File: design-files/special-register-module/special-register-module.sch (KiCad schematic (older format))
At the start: 64 parts, among them U402 74HCT377, U403 74HCT161, U404 74HCT161, U405 74HCT245, U406 74HCT245, U407 74HCT08, U408 74HCT273, U409 74HCT245

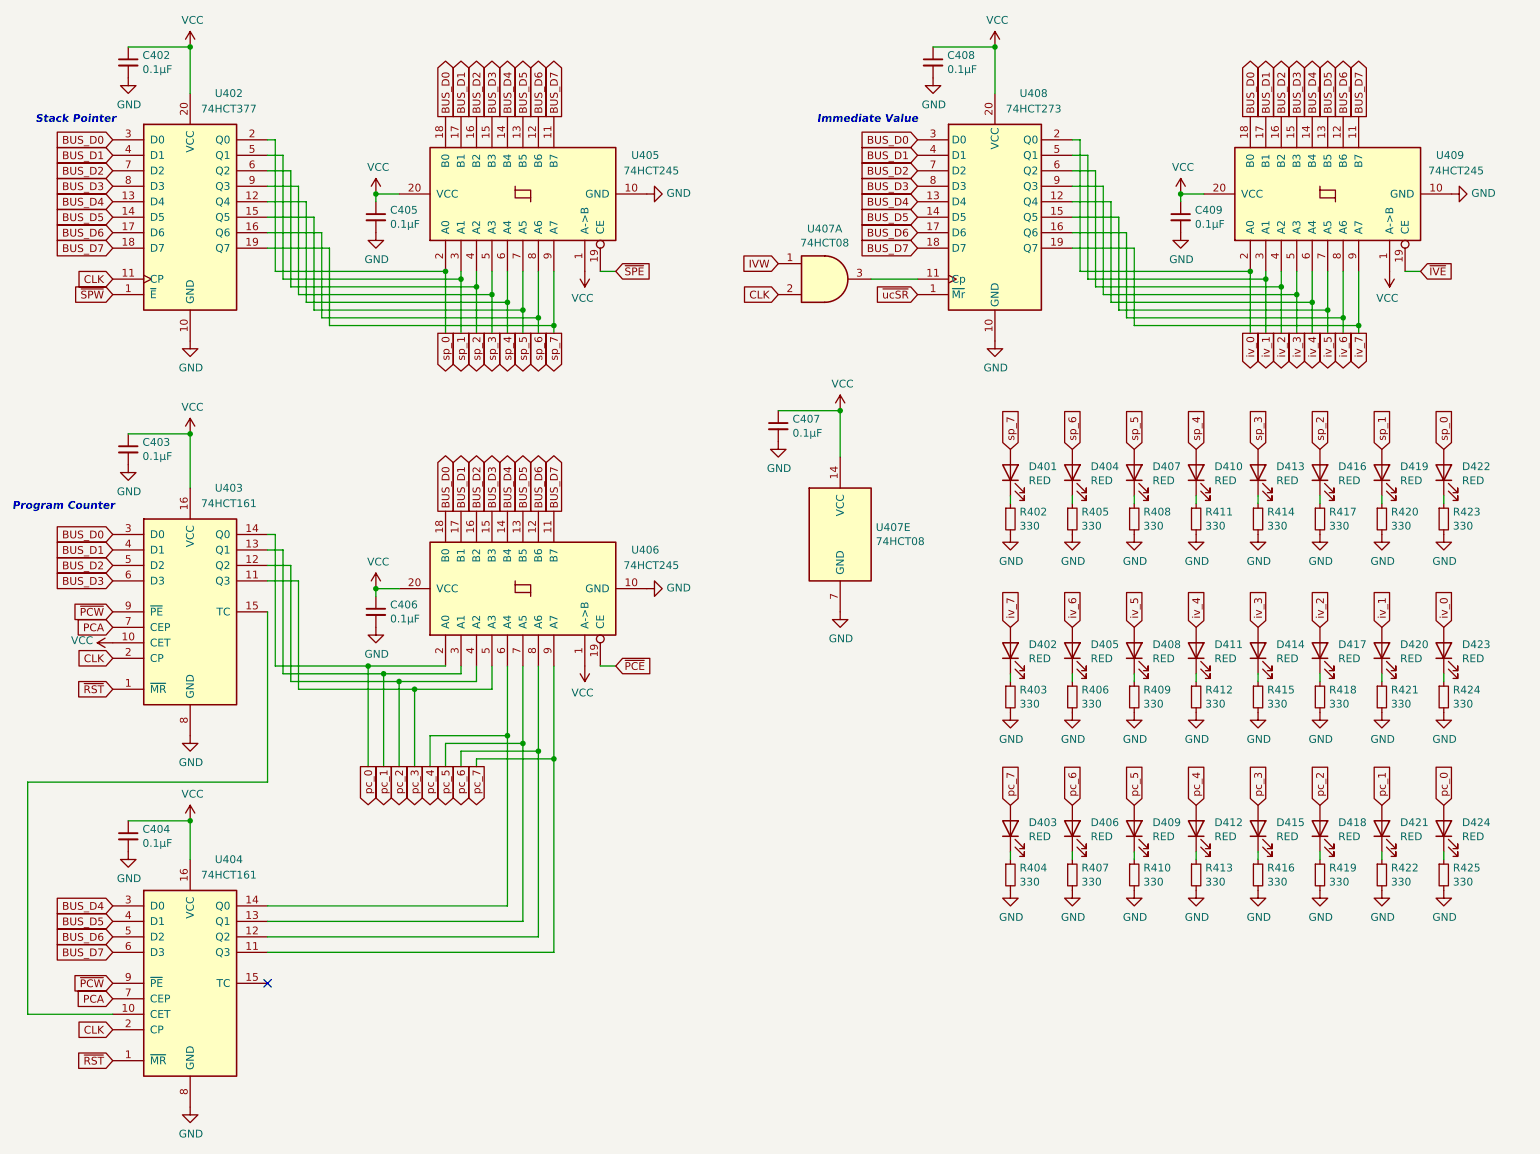
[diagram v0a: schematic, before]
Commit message: Rework to use DIP resistor packs for the LEDs.
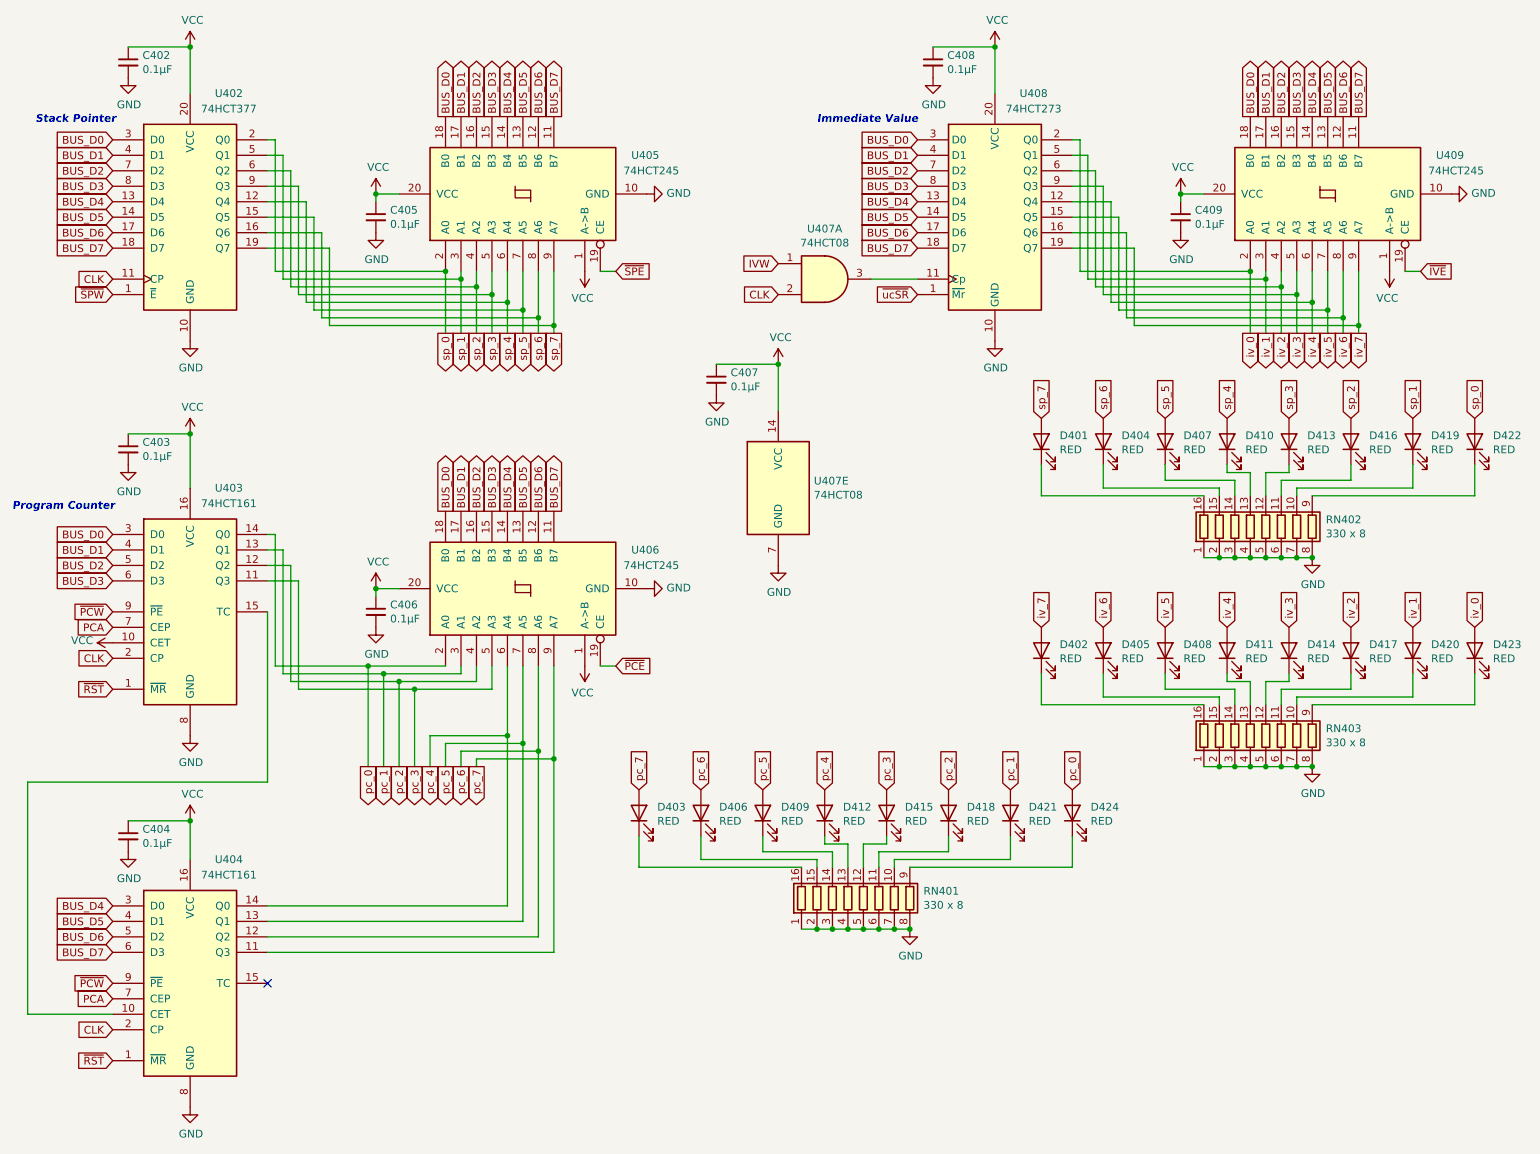
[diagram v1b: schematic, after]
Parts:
- removed R402, R403, R404, R405, R406, R407, R408, R409, R410, R411, R412, R413, R414, R415, R416, R417, R418, R419, R420, R421, R422, R423, R424, R425: 330, Resistor_THT:R_Axial_DIN0204_L3.6mm_D1.6mm_P5.08mm_Horizontal, symbol Device:R_Small
- added RN401, RN402, RN403: 330 x 8, Package_DIP:DIP-16_W7.62mm_Socket, symbol Device:R_Pack08
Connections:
- net GND: now also RN401.1 (R1.1), RN401.2 (R2.1), RN401.3 (R3.1), RN401.4 (R4.1), RN401.5 (R5.1), RN401.6 (R6.1), RN401.7 (R7.1), RN401.8 (R8.1), RN402.1 (R1.1), RN402.2 (R2.1), RN402.3 (R3.1), RN402.4 (R4.1), RN402.5 (R5.1), RN402.6 (R6.1), RN402.7 (R7.1), RN402.8 (R8.1), RN403.1 (R1.1), RN403.2 (R2.1), RN403.3 (R3.1), RN403.4 (R4.1), RN403.5 (R5.1), RN403.6 (R6.1), RN403.7 (R7.1), RN403.8 (R8.1)
- net at D401.1 (K): now also RN402.16 (R1.2)
- net at D404.1 (K): now also RN402.15 (R2.2)
- net at D407.1 (K): now also RN402.14 (R3.2)
- net at D410.1 (K): now also RN402.13 (R4.2)
- net at D413.1 (K): now also RN402.12 (R5.2)
- net at D416.1 (K): now also RN402.11 (R6.2)
- net at D419.1 (K): now also RN402.10 (R7.2)
- net at D422.1 (K): now also RN402.9 (R8.2)
- net at D402.1 (K): now also RN403.16 (R1.2)
- net at D405.1 (K): now also RN403.15 (R2.2)
- net at D408.1 (K): now also RN403.14 (R3.2)
- net at D411.1 (K): now also RN403.13 (R4.2)
- net at D414.1 (K): now also RN403.12 (R5.2)
- net at D417.1 (K): now also RN403.11 (R6.2)
- net at D420.1 (K): now also RN403.10 (R7.2)
- net at D423.1 (K): now also RN403.9 (R8.2)
- net at D403.1 (K): now also RN401.16 (R1.2)
- net at D406.1 (K): now also RN401.15 (R2.2)
- net at D409.1 (K): now also RN401.14 (R3.2)
- net at D412.1 (K): now also RN401.13 (R4.2)
- net at D415.1 (K): now also RN401.12 (R5.2)
- net at D418.1 (K): now also RN401.11 (R6.2)
- net at D421.1 (K): now also RN401.10 (R7.2)
- net at D424.1 (K): now also RN401.9 (R8.2)
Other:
- moved on the sheet: C407, D401, D402, D403, D404, D405, D406, D407, D408, D409, D410, D411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

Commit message: Make the IV register a '377; there isn't really any reason to make it reset to 0 at the beginning of each instruction.
While here, fix the CC selector; Enable is active-low.
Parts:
- removed C407: 0.1µF, Capacitor_THT:C_Radial_D6.3mm_H5.0mm_P2.50mm, symbol Device:C_Small
- removed U407: 74HCT08, Package_DIP:DIP-14_W7.62mm_Socket, symbol 74xx:74LS08
- removed U408: 74HCT273, Package_DIP:DIP-20_W7.62mm_Socket, symbol 74xx:74LS273
- added U407: 74HCT377, symbol 74xx:74LS377
- renumbered U409 to U408
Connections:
- net BUS_D0: now also U407.3 (D0)
- net BUS_D1: now also U407.4 (D1)
- net BUS_D2: now also U407.7 (D2)
- net BUS_D3: now also U407.8 (D3)
- net BUS_D4: now also U407.13 (D4)
- net BUS_D5: now also U407.14 (D5)
- net BUS_D6: now also U407.17 (D6)
- net BUS_D7: now also U407.18 (D7)
- net CLK: now also U407.11 (CP)
- net GND: now also U407.10 (GND)
- net VCC: now also U407.20 (VCC)
- net iv_0: now also U407.2 (Q0)
- net iv_1: now also U407.5 (Q1)
- net iv_2: now also U407.6 (Q2)
- net iv_3: now also U407.9 (Q3)
- net iv_4: now also U407.12 (Q4)
- net iv_5: now also U407.15 (Q5)
- net iv_6: now also U407.16 (Q6)
- net iv_7: now also U407.19 (Q7)
- new net ~IVW: U407.1 (~E)
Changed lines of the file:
@@
 BUS_D7
 $Comp
-L 74xx:74LS245 U409
+L 74xx:74LS245 U408
 U 1 1 61BE426D
 P 9200 1700
-F 0 "U409" V 9450 1000 50  0000 R CNN
+F 0 "U408" V 9450 1000 50  0000 R CNN
 F 1 "74HCT245" V 9350 1050 50  0000 R CNN
 F 2 "Package_DIP:DIP-20_W7.62mm_Socket" H 9200 1700 50  0001 C CNN
@@
 Text GLabel 6550 2050 0    50   Input ~ 0
 BUS_D7
-Text GLabel 5650 2350 0    50   Input ~ 0
+Text GLabel 6550 2250 0    50   Input ~ 0
 CLK
-Text GLabel 5650 2150 0    50   Input ~ 0
-IVW
+Text GLabel 6550 2350 0    50   Input ~ 0
+~IVW
 Text GLabel 9800 2200 2    50   Input ~ 0
 ~IVE
@@
 Text GLabel 9400 1200 1    50   Output ~ 0
 BUS_D7
-$Comp
-L 74xx:74LS273 U408
-U 1 1 61BE6AF1
-P 7050 1850
-F 0 "U408" H 7300 2650 50  0000 C CNN
-F 1 "74HCT273" H 7300 2550 50  0000 C CNN
-F 2 "Package_DIP:DIP-20_W7.62mm_Socket" H 7050 1850 50  0001 C CNN
-F 3 "http://www.ti.com/lit/gpn/sn74LS273" H 7050 1850 50  0001 C CNN
-	1    7050 1850
-	1    0    0    -1
-$EndComp
-$Comp
-L 74xx:74LS08 U407
-U 1 1 61BE8065
-P 5950 2250
-F 0 "U407" H 5950 2575 50  0000 C CNN
-F 1 "74HCT08" H 5950 2484 50  0000 C CNN
-F 2 "Package_DIP:DIP-14_W7.62mm_Socket" H 5950 2250 50  0001 C CNN
-F 3 "http://www.ti.com/lit/gpn/sn74LS08" H 5950 2250 50  0001 C CNN
-	1    5950 2250
-	1    0    0    -1
-$EndComp
-Wire Wire Line
-	6250 2250 6550 2250
-Text GLabel 6550 2350 0    50   Input ~ 0
+Text GLabel 1250 2850 0    50   Input ~ 0
 ~ucSR
 Text Notes 850  1250 0    50   Italic 10
@@
 pc_7
 $Comp
-L 74xx:74LS08 U407
-U 5 1 61D03C75
-P 5650 3600
-F 0 "U407" H 5880 3646 50  0000 L CNN
-F 1 "74HCT08" H 5880 3555 50  0000 L CNN
-F 2 "Package_DIP:DIP-14_W7.62mm_Socket" H 5650 3600 50  0001 C CNN
-F 3 "http://www.ti.com/lit/gpn/sn74LS08" H 5650 3600 50  0001 C CNN
-	5    5650 3600
-	1    0    0    -1
-$EndComp
-$Comp
-L power:GND #PWR0136
-U 1 1 61D077EE
-P 5650 4100
-F 0 "#PWR0136" H 5650 3850 50  0001 C CNN
-F 1 "GND" H 5655 3927 50  0000 C CNN
-F 2 "" H 5650 4100 50  0001 C CNN
-F 3 "" H 5650 4100 50  0001 C CNN
-	1    5650 4100
-	1    0    0    -1
-$EndComp
-$Comp
 L Device:C_Small C402
 U 1 1 61D13B27
@@
 Connection ~ 7050 750
 $Comp
-L Device:C_Small C407
-U 1 1 61D67E66
-P 5250 2900
-F 0 "C407" H 5342 2946 50  0000 L CNN
-F 1 "0.1µF" H 5342 2855 50  0000 L CNN
-F 2 "Capacitor_THT:C_Radial_D6.3mm_H5.0mm_P2.50mm" H 5250 2900 50  0001 C CNN
-F 3 "~" H 5250 2900 50  0001 C CNN
-F 4 "80-C320C104K2R5TA" H 5250 2900 50  0001 C CNN "Mouser"
-	1    5250 2900
-	1    0    0    -1
-$EndComp
-$Comp
-L power:GND #PWR0145
-U 1 1 61D67E6C
-P 5250 3000
-F 0 "#PWR0145" H 5250 2750 50  0001 C CNN
-F 1 "GND" H 5255 2827 50  0000 C CNN
-F 2 "" H 5250 3000 50  0001 C CNN
-F 3 "" H 5250 3000 50  0001 C CNN
-	1    5250 3000
-	1    0    0    -1
-$EndComp
-Wire Wire Line
-	5650 3100 5650 2800
-Wire Wire Line
-	5650 2800 5250 2800
-$Comp
-L power:VCC #PWR0146
-U 1 1 61D67E74
-P 5650 2800
-F 0 "#PWR0146" H 5650 2650 50  0001 C CNN
-F 1 "VCC" H 5665 2973 50  0000 C CNN
-F 2 "" H 5650 2800 50  0001 C CNN
-F 3 "" H 5650 2800 50  0001 C CNN
-	1    5650 2800
-	1    0    0    -1
-$EndComp
-Connection ~ 5650 2800
-$Comp
 L Device:C_Small C405
 U 1 1 61D6F6C2
@@
 Wire Wire Line
 	4750 5850 4750 6050
+$Comp
+L 74xx:74LS377 U407
+U 1 1 66CFD9C5
+P 7050 1850
+F 0 "U407" H 7300 2650 50  0000 C CNN
+F 1 "74HCT377" H 7300 2550 50  0000 C CNN
+F 2 "" H 7050 1850 50  0001 C CNN
+F 3 "http://www.ti.com/lit/gpn/sn74LS377" H 7050 1850 50  0001 C CNN
+	1    7050 1850
+	1    0    0    -1
+$EndComp
 $EndSCHEMATC
